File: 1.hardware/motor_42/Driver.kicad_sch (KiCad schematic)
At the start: 0 parts

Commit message: 중간 저장
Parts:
- added C24, C25, C26, C27: 0.1uF/50V, symbol Device:C_Small_US
- added IC1, IC2: TB67H450FNG,EL, SOIC127P600X175-9N, symbol SamacSys_Parts:TB67H450FNG,EL
- added R14, R15: 0.1/0.25w, symbol Device:R_Small_US
- added R16, R17, R18, R19: 1k/0.063w, symbol Device:R_Small_US
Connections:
- new net: C27.1, R18.2, R19.1
- new net: IC2.7 (RS), R15.2
- new net: C24.1, R16.2, R17.1
- new net: IC1.7 (RS), R14.2
- new net GND: C24.2, C25.2, C26.2, C27.2, IC1.1 (GND), IC1.9 (EP), IC2.1 (GND), IC2.9 (EP), R14.1, R15.1
- new net IN_A+: IC1.3 (IN1)
- new net IN_A-: IC1.2 (IN2)
- new net IN_B+: IC2.3 (IN1)
- new net IN_B-: IC2.2 (IN2)
- new net OUT_A+: IC1.6 (OUT1)
- new net OUT_A-: IC1.8 (OUT2)
- new net OUT_B+: IC2.6 (OUT1)
- new net OUT_B-: IC2.8 (OUT2)
- new net VCC: IC1.5 (VM), IC2.5 (VM)
- new net VREF_A: C25.1, IC1.4 (VREF), R16.1
- new net VREF_B: C26.1, IC2.4 (VREF), R18.1
- new net VREF_PWM_A: R17.2
- new net VREF_PWM_B: R19.2

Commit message: 중간 저장
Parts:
- renumbered C24 to C22, C25 to C23, C27 to C24, C26 to C25, R17 to R12, R16 to R13, R19 to R14, R18 to R15, R14 to R16, R15 to R17
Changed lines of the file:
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@@
 		(on_board yes)
 		(dnp no)
-		(property "Reference" "R19"
+		(property "Reference" "R14"
 			(at 113.538 28.702 90)
 			(effects
@@
 			(project "motor_42"
 				(path "/3c5de6a8-6840-43a5-a2fb-24dbb7f0450d/a4b26d4c-a648-4a1c-b008-d85c88bc1a9d"
-					(reference "R19")
+					(reference "R14")
 					(unit 1)
 				)
@@
 		(on_board yes)
 		(dnp no)
-		(property "Reference" "R15"
+		(property "Reference" "R17"
 			(at 141.478 62.738 0)
 			(effects
@@
 			(project "motor_42"
 				(path "/3c5de6a8-6840-43a5-a2fb-24dbb7f0450d/a4b26d4c-a648-4a1c-b008-d85c88bc1a9d"
-					(reference "R15")
+					(reference "R17")
 					(unit 1)
 				)
@@
 		(on_board yes)
 		(dnp no)
-		(property "Reference" "C26"
+		(property "Reference" "C25"
 			(at 133.35 30.6069 0)
 			(effects
@@
 			(project "motor_42"
 				(path "/3c5de6a8-6840-43a5-a2fb-24dbb7f0450d/a4b26d4c-a648-4a1c-b008-d85c88bc1a9d"
-					(reference "C26")
+					(reference "C25")
 					(unit 1)
 				)
@@
 		(on_board yes)
 		(dnp no)
-		(property "Reference" "C24"
+		(property "Reference" "C22"
 			(at 50.8 30.6069 0)
 			(effects
@@
 			(project "motor_42"
 				(path "/3c5de6a8-6840-43a5-a2fb-24dbb7f0450d/a4b26d4c-a648-4a1c-b008-d85c88bc1a9d"
-					(reference "C24")
+					(reference "C22")
 					(unit 1)
 				)
@@
 		(on_board yes)
 		(dnp no)
-		(property "Reference" "#PWR037"
+		(property "Reference" "#PWR029"
 			(at 130.81 43.18 0)
 			(effects
@@
 			(project "motor_42"
 				(path "/3c5de6a8-6840-43a5-a2fb-24dbb7f0450d/a4b26d4c-a648-4a1c-b008-d85c88bc1a9d"
-					(reference "#PWR037")
+					(reference "#PWR029")
 					(unit 1)
 				)
@@
 		(on_board yes)
 		(dnp no)
-		(property "Reference" "C27"
+		(property "Reference" "C24"
 			(at 123.19 30.6069 0)
 			(effects
@@
 			(project "motor_42"
 				(path "/3c5de6a8-6840-43a5-a2fb-24dbb7f0450d/a4b26d4c-a648-4a1c-b008-d85c88bc1a9d"
-					(reference "C27")
+					(reference "C24")
 					(unit 1)
 				)
@@
 		(on_board yes)
 		(dnp no)
-		(property "Reference" "#PWR036"
+		(property "Reference" "#PWR031"
 			(at 123.19 82.55 0)
 			(effects
@@
 			(project "motor_42"
 				(path "/3c5de6a8-6840-43a5-a2fb-24dbb7f0450d/a4b26d4c-a648-4a1c-b008-d85c88bc1a9d"
-					(reference "#PWR036")
+					(reference "#PWR031")
 					(unit 1)
 				)
@@
 		(on_board yes)
 		(dnp no)
-		(property "Reference" "R18"
+		(property "Reference" "R15"
 			(at 123.698 28.702 90)
 			(effects
@@
 			(project "motor_42"
 				(path "/3c5de6a8-6840-43a5-a2fb-24dbb7f0450d/a4b26d4c-a648-4a1c-b008-d85c88bc1a9d"
-					(reference "R18")
+					(reference "R15")
 					(unit 1)
 				)
@@
 		(on_board yes)
 		(dnp no)
-		(property "Reference" "#PWR040"
+		(property "Reference" "#PWR026"
 			(at 48.26 43.18 0)
 			(effects
@@
 			(project "motor_42"
 				(path "/3c5de6a8-6840-43a5-a2fb-24dbb7f0450d/a4b26d4c-a648-4a1c-b008-d85c88bc1a9d"
-					(reference "#PWR040")
+					(reference "#PWR026")
 					(unit 1)
 				)
@@
 		(on_board yes)
 		(dnp no)
-		(property "Reference" "#PWR038"
+		(property "Reference" "#PWR028"
 			(at 120.65 43.18 0)
 			(effects
@@
 			(project "motor_42"
 				(path "/3c5de6a8-6840-43a5-a2fb-24dbb7f0450d/a4b26d4c-a648-4a1c-b008-d85c88bc1a9d"
-					(reference "#PWR038")
+					(reference "#PWR028")
 					(unit 1)
 				)
@@
 		(on_board yes)
 		(dnp no)
-		(property "Reference" "R17"
+		(property "Reference" "R12"
 			(at 41.148 28.702 90)
 			(effects
@@
 			(project "motor_42"
 				(path "/3c5de6a8-6840-43a5-a2fb-24dbb7f0450d/a4b26d4c-a648-4a1c-b008-d85c88bc1a9d"
-					(reference "R17")
+					(reference "R12")
 					(unit 1)
 				)
@@
 		(on_board yes)
 		(dnp no)
-		(property "Reference" "R16"
+		(property "Reference" "R13"
 			(at 51.308 28.702 90)
 			(effects
@@
 			(project "motor_42"
 				(path "/3c5de6a8-6840-43a5-a2fb-24dbb7f0450d/a4b26d4c-a648-4a1c-b008-d85c88bc1a9d"
-					(reference "R16")
+					(reference "R13")
 					(unit 1)
 				)
@@
 		(on_board yes)
 		(dnp no)
-		(property "Reference" "#PWR035"
+		(property "Reference" "#PWR030"
 			(at 50.8 82.55 0)
 			(effects
@@
 			(project "motor_42"
 				(path "/3c5de6a8-6840-43a5-a2fb-24dbb7f0450d/a4b26d4c-a648-4a1c-b008-d85c88bc1a9d"
-					(reference "#PWR035")
+					(reference "#PWR030")
 					(unit 1)
 				)
@@
 		(on_board yes)
 		(dnp no)
-		(property "Reference" "#PWR039"
+		(property "Reference" "#PWR027"
 			(at 58.42 43.18 0)
 			(effects
@@
 			(project "motor_42"
 				(path "/3c5de6a8-6840-43a5-a2fb-24dbb7f0450d/a4b26d4c-a648-4a1c-b008-d85c88bc1a9d"
-					(reference "#PWR039")
+					(reference "#PWR027")
 					(unit 1)
 				)
@@
 		(on_board yes)
 		(dnp no)
-		(property "Reference" "R14"
+		(property "Reference" "R16"
 			(at 67.818 62.738 0)
 			(effects
@@
 			(project "motor_42"
 				(path "/3c5de6a8-6840-43a5-a2fb-24dbb7f0450d/a4b26d4c-a648-4a1c-b008-d85c88bc1a9d"
-					(reference "R14")
+					(reference "R16")
 					(unit 1)
 				)
@@
 		(on_board yes)
 		(dnp no)
-		(property "Reference" "C25"
+		(property "Reference" "C23"
 			(at 60.96 30.6069 0)
 			(effects
@@
 			(project "motor_42"
 				(path "/3c5de6a8-6840-43a5-a2fb-24dbb7f0450d/a4b26d4c-a648-4a1c-b008-d85c88bc1a9d"
-					(reference "C25")
-					(unit 1)
-				)
+					(reference "C23")
+					(unit 1)
+				)

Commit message: 회로도 대충 완성
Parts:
- IC1, IC2: footprint SOIC127P600X175-9N -> SamacSys_Parts:SOIC127P600X175-9N
- R18: renamed from R12; footprint (none) -> Resistor_SMD:R_0402_1005Metric
- R19: renamed from R13; footprint (none) -> Resistor_SMD:R_0402_1005Metric
- R21: renamed from R14; footprint (none) -> Resistor_SMD:R_0402_1005Metric
- R22: renamed from R15; footprint (none) -> Resistor_SMD:R_0402_1005Metric
- renumbered C22 to C24, C23 to C25, C24 to C26, C25 to C27, R16 to R20, R17 to R23
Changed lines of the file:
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@@
 		(on_board yes)
 		(dnp no)
-		(property "Reference" "R14"
+		(property "Reference" "R21"
 			(at 113.538 28.702 90)
 			(effects
@@
 			)
 		)
-		(property "Footprint" ""
+		(property "Footprint" "Resistor_SMD:R_0402_1005Metric"
 			(at 115.57 26.67 0)
 			(effects
@@
 			(project "motor_42"
 				(path "/3c5de6a8-6840-43a5-a2fb-24dbb7f0450d/a4b26d4c-a648-4a1c-b008-d85c88bc1a9d"
-					(reference "R14")
+					(reference "R21")
 					(unit 1)
 				)
@@
 		(on_board yes)
 		(dnp no)
-		(property "Reference" "R17"
+		(property "Reference" "R23"
 			(at 141.478 62.738 0)
 			(effects
@@
 			(project "motor_42"
 				(path "/3c5de6a8-6840-43a5-a2fb-24dbb7f0450d/a4b26d4c-a648-4a1c-b008-d85c88bc1a9d"
-					(reference "R17")
+					(reference "R23")
 					(unit 1)
 				)
@@
 		(on_board yes)
 		(dnp no)
-		(property "Reference" "C25"
+		(property "Reference" "C27"
 			(at 133.35 30.6069 0)
 			(effects
@@
 			(project "motor_42"
 				(path "/3c5de6a8-6840-43a5-a2fb-24dbb7f0450d/a4b26d4c-a648-4a1c-b008-d85c88bc1a9d"
-					(reference "C25")
+					(reference "C27")
 					(unit 1)
 				)
@@
 		(on_board yes)
 		(dnp no)
-		(property "Reference" "C22"
+		(property "Reference" "C24"
 			(at 50.8 30.6069 0)
 			(effects
@@
 			(project "motor_42"
 				(path "/3c5de6a8-6840-43a5-a2fb-24dbb7f0450d/a4b26d4c-a648-4a1c-b008-d85c88bc1a9d"
-					(reference "C22")
+					(reference "C24")
 					(unit 1)
 				)
@@
 		(on_board yes)
 		(dnp no)
-		(property "Reference" "#PWR029"
+		(property "Reference" "#PWR033"
 			(at 130.81 43.18 0)
 			(effects
@@
 			(project "motor_42"
 				(path "/3c5de6a8-6840-43a5-a2fb-24dbb7f0450d/a4b26d4c-a648-4a1c-b008-d85c88bc1a9d"
-					(reference "#PWR029")
+					(reference "#PWR033")
 					(unit 1)
 				)
@@
 		(on_board yes)
 		(dnp no)
-		(property "Reference" "C24"
+		(property "Reference" "C26"
 			(at 123.19 30.6069 0)
 			(effects
@@
 			(project "motor_42"
 				(path "/3c5de6a8-6840-43a5-a2fb-24dbb7f0450d/a4b26d4c-a648-4a1c-b008-d85c88bc1a9d"
-					(reference "C24")
+					(reference "C26")
 					(unit 1)
 				)
@@
 		(on_board yes)
 		(dnp no)
-		(property "Reference" "#PWR031"
+		(property "Reference" "#PWR032"
 			(at 123.19 82.55 0)
 			(effects
@@
 			(project "motor_42"
 				(path "/3c5de6a8-6840-43a5-a2fb-24dbb7f0450d/a4b26d4c-a648-4a1c-b008-d85c88bc1a9d"
-					(reference "#PWR031")
+					(reference "#PWR032")
 					(unit 1)
 				)
@@
 		(on_board yes)
 		(dnp no)
-		(property "Reference" "R15"
+		(property "Reference" "R22"
 			(at 123.698 28.702 90)
 			(effects
@@
 			)
 		)
-		(property "Footprint" ""
+		(property "Footprint" "Resistor_SMD:R_0402_1005Metric"
 			(at 125.73 26.67 0)
 			(effects
@@
 			(project "motor_42"
 				(path "/3c5de6a8-6840-43a5-a2fb-24dbb7f0450d/a4b26d4c-a648-4a1c-b008-d85c88bc1a9d"
-					(reference "R15")
+					(reference "R22")
 					(unit 1)
 				)
@@
 			)
 		)
-		(property "Footprint" "SOIC127P600X175-9N"
+		(property "Footprint" "SamacSys_Parts:SOIC127P600X175-9N"
 			(at 134.62 48.26 0)
 			(effects
@@
 		(on_board yes)
 		(dnp no)
-		(property "Reference" "#PWR026"
+		(property "Reference" "#PWR028"
 			(at 48.26 43.18 0)
 			(effects
@@
 			(project "motor_42"
 				(path "/3c5de6a8-6840-43a5-a2fb-24dbb7f0450d/a4b26d4c-a648-4a1c-b008-d85c88bc1a9d"
-					(reference "#PWR026")
+					(reference "#PWR028")
 					(unit 1)
 				)
@@
 		(on_board yes)
 		(dnp no)
-		(property "Reference" "#PWR028"
+		(property "Reference" "#PWR031"
 			(at 120.65 43.18 0)
 			(effects
@@
 			(project "motor_42"
 				(path "/3c5de6a8-6840-43a5-a2fb-24dbb7f0450d/a4b26d4c-a648-4a1c-b008-d85c88bc1a9d"
-					(reference "#PWR028")
+					(reference "#PWR031")
 					(unit 1)
 				)
@@
 		(on_board yes)
 		(dnp no)
-		(property "Reference" "R12"
+		(property "Reference" "R18"
 			(at 41.148 28.702 90)
 			(effects
@@
 			)
 		)
-		(property "Footprint" ""
+		(property "Footprint" "Resistor_SMD:R_0402_1005Metric"
 			(at 43.18 26.67 0)
 			(effects
@@
 			(project "motor_42"
 				(path "/3c5de6a8-6840-43a5-a2fb-24dbb7f0450d/a4b26d4c-a648-4a1c-b008-d85c88bc1a9d"
-					(reference "R12")
+					(reference "R18")
 					(unit 1)
 				)
@@
 		(on_board yes)
 		(dnp no)
-		(property "Reference" "R13"
+		(property "Reference" "R19"
 			(at 51.308 28.702 90)
 			(effects
@@
 			)
 		)
-		(property "Footprint" ""
+		(property "Footprint" "Resistor_SMD:R_0402_1005Metric"
 			(at 53.34 26.67 0)
 			(effects
@@
 			(project "motor_42"
 				(path "/3c5de6a8-6840-43a5-a2fb-24dbb7f0450d/a4b26d4c-a648-4a1c-b008-d85c88bc1a9d"
-					(reference "R13")
+					(reference "R19")
 					(unit 1)
 				)
@@
 		(on_board yes)
 		(dnp no)
-		(property "Reference" "#PWR030"
+		(property "Reference" "#PWR029"
 			(at 50.8 82.55 0)
 			(effects
@@
 			(project "motor_42"
 				(path "/3c5de6a8-6840-43a5-a2fb-24dbb7f0450d/a4b26d4c-a648-4a1c-b008-d85c88bc1a9d"
-					(reference "#PWR030")
+					(reference "#PWR029")
 					(unit 1)
 				)
@@
 		(on_board yes)
 		(dnp no)
-		(property "Reference" "#PWR027"
+		(property "Reference" "#PWR030"
 			(at 58.42 43.18 0)
 			(effects
@@
 			(project "motor_42"
 				(path "/3c5de6a8-6840-43a5-a2fb-24dbb7f0450d/a4b26d4c-a648-4a1c-b008-d85c88bc1a9d"
-					(reference "#PWR027")
+					(reference "#PWR030")
 					(unit 1)
 				)
@@
 		(on_board yes)
 		(dnp no)
-		(property "Reference" "R16"
+		(property "Reference" "R20"
 			(at 67.818 62.738 0)
 			(effects
@@
 			(project "motor_42"
 				(path "/3c5de6a8-6840-43a5-a2fb-24dbb7f0450d/a4b26d4c-a648-4a1c-b008-d85c88bc1a9d"
-					(reference "R16")
+					(reference "R20")
 					(unit 1)
 				)
@@
 		(on_board yes)
 		(dnp no)
-		(property "Reference" "C23"
+		(property "Reference" "C25"
 			(at 60.96 30.6069 0)
 			(effects
@@
 			(project "motor_42"
 				(path "/3c5de6a8-6840-43a5-a2fb-24dbb7f0450d/a4b26d4c-a648-4a1c-b008-d85c88bc1a9d"
-					(reference "C23")
+					(reference "C25")
 					(unit 1)
 				)
@@
 			)
 		)
-		(property "Footprint" "SOIC127P600X175-9N"
+		(property "Footprint" "SamacSys_Parts:SOIC127P600X175-9N"
 			(at 62.23 48.26 0)
 			(effects

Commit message: 수정
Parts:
- C24, C25, C26, C27: footprint (none) -> Capacitor_SMD:C_0402_1005Metric
- R20, R23: footprint (none) -> Resistor_SMD:R_1206_3216Metric
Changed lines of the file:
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@@
 			)
 		)
-		(property "Footprint" ""
+		(property "Footprint" "Resistor_SMD:R_1206_3216Metric"
 			(at 143.51 64.77 0)
 			(effects
@@
 			)
 		)
-		(property "Footprint" ""
+		(property "Footprint" "Capacitor_SMD:C_0402_1005Metric"
 			(at 130.81 31.75 0)
 			(effects
@@
 			)
 		)
-		(property "Footprint" ""
+		(property "Footprint" "Capacitor_SMD:C_0402_1005Metric"
 			(at 48.26 31.75 0)
 			(effects
@@
 			)
 		)
-		(property "Footprint" ""
+		(property "Footprint" "Capacitor_SMD:C_0402_1005Metric"
 			(at 120.65 31.75 0)
 			(effects
@@
 			)
 		)
-		(property "Footprint" ""
+		(property "Footprint" "Resistor_SMD:R_1206_3216Metric"
 			(at 69.85 64.77 0)
 			(effects
@@
 			)
 		)
-		(property "Footprint" ""
+		(property "Footprint" "Capacitor_SMD:C_0402_1005Metric"
 			(at 58.42 31.75 0)
 			(effects

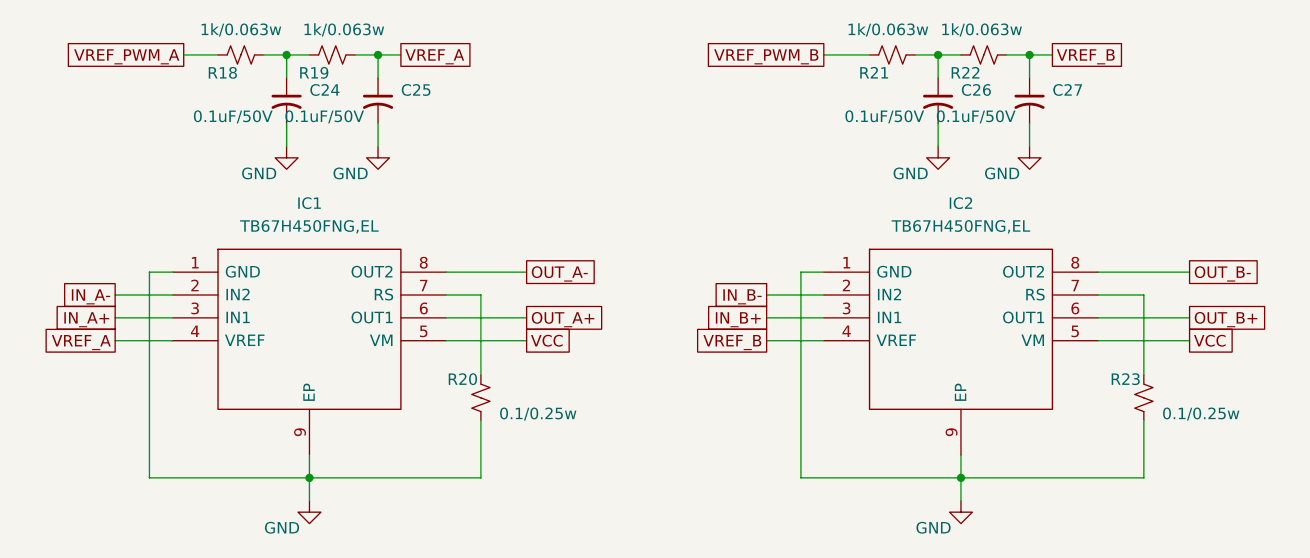
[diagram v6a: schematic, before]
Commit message: 번호 초기화 및 led 변경
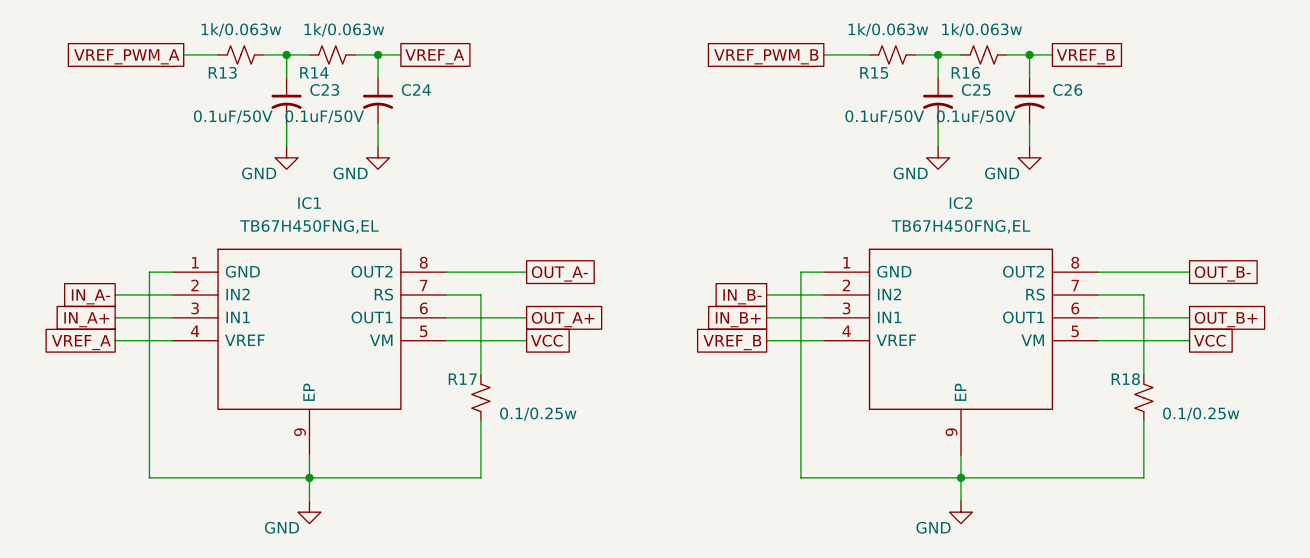
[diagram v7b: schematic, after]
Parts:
- renumbered C24 to C23, C25 to C24, C26 to C25, C27 to C26, R18 to R13, R19 to R14, R21 to R15, R22 to R16, R20 to R17, R23 to R18
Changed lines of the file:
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@@
 		(on_board yes)
 		(dnp no)
-		(property "Reference" "R21"
+		(property "Reference" "R15"
 			(at 113.538 28.702 90)
 			(effects
@@
 			(project "motor_42"
 				(path "/3c5de6a8-6840-43a5-a2fb-24dbb7f0450d/a4b26d4c-a648-4a1c-b008-d85c88bc1a9d"
-					(reference "R21")
+					(reference "R15")
 					(unit 1)
 				)
@@
 		(on_board yes)
 		(dnp no)
-		(property "Reference" "R23"
+		(property "Reference" "R18"
 			(at 141.478 62.738 0)
 			(effects
@@
 			(project "motor_42"
 				(path "/3c5de6a8-6840-43a5-a2fb-24dbb7f0450d/a4b26d4c-a648-4a1c-b008-d85c88bc1a9d"
-					(reference "R23")
+					(reference "R18")
 					(unit 1)
 				)
@@
 		(on_board yes)
 		(dnp no)
-		(property "Reference" "C27"
+		(property "Reference" "C26"
 			(at 133.35 30.6069 0)
 			(effects
@@
 			(project "motor_42"
 				(path "/3c5de6a8-6840-43a5-a2fb-24dbb7f0450d/a4b26d4c-a648-4a1c-b008-d85c88bc1a9d"
-					(reference "C27")
+					(reference "C26")
 					(unit 1)
 				)
@@
 		(on_board yes)
 		(dnp no)
-		(property "Reference" "C24"
+		(property "Reference" "C23"
 			(at 50.8 30.6069 0)
 			(effects
@@
 			(project "motor_42"
 				(path "/3c5de6a8-6840-43a5-a2fb-24dbb7f0450d/a4b26d4c-a648-4a1c-b008-d85c88bc1a9d"
-					(reference "C24")
+					(reference "C23")
 					(unit 1)
 				)
@@
 		(on_board yes)
 		(dnp no)
-		(property "Reference" "#PWR033"
+		(property "Reference" "#PWR029"
 			(at 130.81 43.18 0)
 			(effects
@@
 			(project "motor_42"
 				(path "/3c5de6a8-6840-43a5-a2fb-24dbb7f0450d/a4b26d4c-a648-4a1c-b008-d85c88bc1a9d"
-					(reference "#PWR033")
+					(reference "#PWR029")
 					(unit 1)
 				)
@@
 		(on_board yes)
 		(dnp no)
-		(property "Reference" "C26"
+		(property "Reference" "C25"
 			(at 123.19 30.6069 0)
 			(effects
@@
 			(project "motor_42"
 				(path "/3c5de6a8-6840-43a5-a2fb-24dbb7f0450d/a4b26d4c-a648-4a1c-b008-d85c88bc1a9d"
-					(reference "C26")
+					(reference "C25")
 					(unit 1)
 				)
@@
 		(on_board yes)
 		(dnp no)
-		(property "Reference" "#PWR032"
+		(property "Reference" "#PWR031"
 			(at 123.19 82.55 0)
 			(effects
@@
 			(project "motor_42"
 				(path "/3c5de6a8-6840-43a5-a2fb-24dbb7f0450d/a4b26d4c-a648-4a1c-b008-d85c88bc1a9d"
-					(reference "#PWR032")
+					(reference "#PWR031")
 					(unit 1)
 				)
@@
 		(on_board yes)
 		(dnp no)
-		(property "Reference" "R22"
+		(property "Reference" "R16"
 			(at 123.698 28.702 90)
 			(effects
@@
 			(project "motor_42"
 				(path "/3c5de6a8-6840-43a5-a2fb-24dbb7f0450d/a4b26d4c-a648-4a1c-b008-d85c88bc1a9d"
-					(reference "R22")
+					(reference "R16")
 					(unit 1)
 				)
@@
 		(on_board yes)
 		(dnp no)
-		(property "Reference" "#PWR028"
+		(property "Reference" "#PWR026"
 			(at 48.26 43.18 0)
 			(effects
@@
 			(project "motor_42"
 				(path "/3c5de6a8-6840-43a5-a2fb-24dbb7f0450d/a4b26d4c-a648-4a1c-b008-d85c88bc1a9d"
-					(reference "#PWR028")
+					(reference "#PWR026")
 					(unit 1)
 				)
@@
 		(on_board yes)
 		(dnp no)
-		(property "Reference" "#PWR031"
+		(property "Reference" "#PWR028"
 			(at 120.65 43.18 0)
 			(effects
@@
 			(project "motor_42"
 				(path "/3c5de6a8-6840-43a5-a2fb-24dbb7f0450d/a4b26d4c-a648-4a1c-b008-d85c88bc1a9d"
-					(reference "#PWR031")
+					(reference "#PWR028")
 					(unit 1)
 				)
@@
 		(on_board yes)
 		(dnp no)
-		(property "Reference" "R18"
+		(property "Reference" "R13"
 			(at 41.148 28.702 90)
 			(effects
@@
 			(project "motor_42"
 				(path "/3c5de6a8-6840-43a5-a2fb-24dbb7f0450d/a4b26d4c-a648-4a1c-b008-d85c88bc1a9d"
-					(reference "R18")
+					(reference "R13")
 					(unit 1)
 				)
@@
 		(on_board yes)
 		(dnp no)
-		(property "Reference" "R19"
+		(property "Reference" "R14"
 			(at 51.308 28.702 90)
 			(effects
@@
 			(project "motor_42"
 				(path "/3c5de6a8-6840-43a5-a2fb-24dbb7f0450d/a4b26d4c-a648-4a1c-b008-d85c88bc1a9d"
-					(reference "R19")
+					(reference "R14")
 					(unit 1)
 				)
@@
 		(on_board yes)
 		(dnp no)
-		(property "Reference" "#PWR029"
+		(property "Reference" "#PWR030"
 			(at 50.8 82.55 0)
 			(effects
@@
 			(project "motor_42"
 				(path "/3c5de6a8-6840-43a5-a2fb-24dbb7f0450d/a4b26d4c-a648-4a1c-b008-d85c88bc1a9d"
-					(reference "#PWR029")
+					(reference "#PWR030")
 					(unit 1)
 				)
@@
 		(on_board yes)
 		(dnp no)
-		(property "Reference" "#PWR030"
+		(property "Reference" "#PWR027"
 			(at 58.42 43.18 0)
 			(effects
@@
 			(project "motor_42"
 				(path "/3c5de6a8-6840-43a5-a2fb-24dbb7f0450d/a4b26d4c-a648-4a1c-b008-d85c88bc1a9d"
-					(reference "#PWR030")
+					(reference "#PWR027")
 					(unit 1)
 				)
@@
 		(on_board yes)
 		(dnp no)
-		(property "Reference" "R20"
+		(property "Reference" "R17"
 			(at 67.818 62.738 0)
 			(effects
@@
 			(project "motor_42"
 				(path "/3c5de6a8-6840-43a5-a2fb-24dbb7f0450d/a4b26d4c-a648-4a1c-b008-d85c88bc1a9d"
-					(reference "R20")
+					(reference "R17")
 					(unit 1)
 				)
@@
 		(on_board yes)
 		(dnp no)
-		(property "Reference" "C25"
+		(property "Reference" "C24"
 			(at 60.96 30.6069 0)
 			(effects
@@
 			(project "motor_42"
 				(path "/3c5de6a8-6840-43a5-a2fb-24dbb7f0450d/a4b26d4c-a648-4a1c-b008-d85c88bc1a9d"
-					(reference "C25")
-					(unit 1)
-				)
+					(reference "C24")
+					(unit 1)
+				)
